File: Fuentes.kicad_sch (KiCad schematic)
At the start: 15 parts, among them J20 Conector 3V3, J21 Conector GND, J43 Conector GND, U1 LM2596S-ADJ, U2 LM1117-3.3

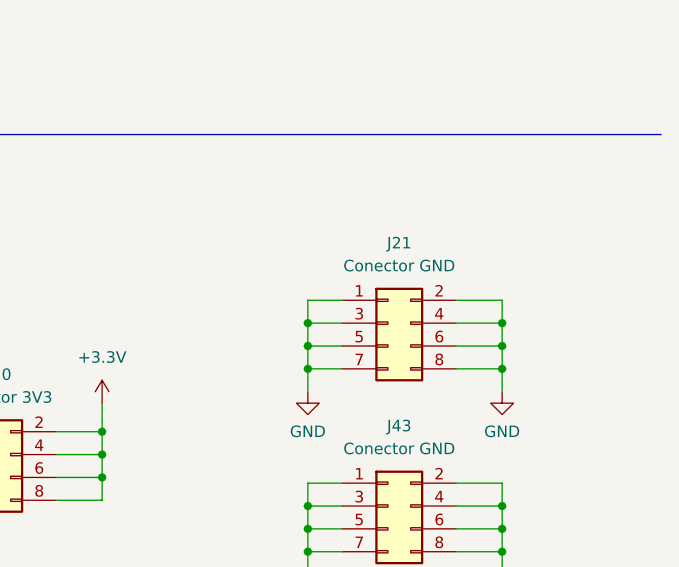
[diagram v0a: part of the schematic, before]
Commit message: Corrección de PCB.
Se agregaron algunos pin headers para conectar a GND algunos puntos. Se generaron los Gerber finales.
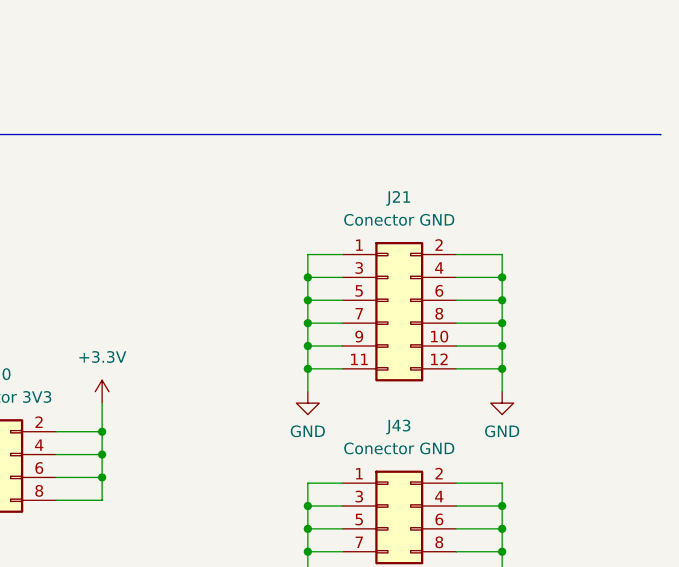
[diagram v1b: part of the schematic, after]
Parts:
- removed J21: Conector GND, Connector_PinHeader_2.54mm:PinHeader_2x04_P2.54mm_Vertical, symbol Connector_Generic:Conn_02x04_Odd_Even
- added J21: Conector GND, Connector_PinHeader_2.54mm:PinHeader_2x06_P2.54mm_Vertical, symbol Connector_Generic:Conn_02x06_Odd_Even
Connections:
- net GND: now also J21.1 (Pin_1), J21.10 (Pin_10), J21.11 (Pin_11), J21.12 (Pin_12), J21.2 (Pin_2), J21.3 (Pin_3), J21.4 (Pin_4), J21.5 (Pin_5), J21.6 (Pin_6), J21.7 (Pin_7), J21.8 (Pin_8), J21.9 (Pin_9)
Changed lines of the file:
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@@
   (junction (at 214.0204 67.31) (diameter 0) (color 0 0 0 0)
   )
+  (junction (at 245.745 109.855) (diameter 0) (color 0 0 0 0)
+  )
   (junction (at 245.745 132.715) (diameter 0) (color 0 0 0 0)
   )
@@
   (junction (at 129.54 67.31) (diameter 0) (color 0 0 0 0)
   )
+  (junction (at 267.335 107.315) (diameter 0) (color 0 0 0 0)
+  )
   (junction (at 267.335 114.935) (diameter 0) (color 0 0 0 0)
   )
@@
   (junction (at 168.91 67.31) (diameter 0) (color 0 0 0 0)
   )
+  (junction (at 267.335 109.855) (diameter 0) (color 0 0 0 0)
+  )
   (junction (at 222.885 129.54) (diameter 0) (color 0 0 0 0)
   )
+  (junction (at 245.745 107.315) (diameter 0) (color 0 0 0 0)
+  )
   (junction (at 267.335 112.395) (diameter 0) (color 0 0 0 0)
   )
+  (wire (pts (xy 249.555 104.775) (xy 245.745 104.775))
+    (stroke (width 0) (type default) (color 0 0 0 0))
+  )
   (wire (pts (xy 201.295 121.92) (xy 201.295 124.46))
     (stroke (width 0) (type default) (color 0 0 0 0))
@@
     (stroke (width 0) (type default) (color 0 0 0 0))
   )
+  (wire (pts (xy 267.335 104.775) (xy 267.335 107.315))
+    (stroke (width 0) (type default) (color 0 0 0 0))
+  )
   (wire (pts (xy 144.78 59.69) (xy 144.78 67.31))
     (stroke (width 0) (type default) (color 0 0 0 0))
   )
+  (wire (pts (xy 262.255 107.315) (xy 267.335 107.315))
+    (stroke (width 0) (type default) (color 0 0 0 0))
+  )
   (wire (pts (xy 262.255 137.795) (xy 267.335 137.795))
     (stroke (width 0) (type default) (color 0 0 0 0))
   )
+  (wire (pts (xy 249.555 107.315) (xy 245.745 107.315))
+    (stroke (width 0) (type default) (color 0 0 0 0))
+  )
   (wire (pts (xy 213.995 54.61) (xy 193.04 54.61))
     (stroke (width 0) (type default) (color 0 0 0 0))
@@
     (stroke (width 0) (type default) (color 0 0 0 0))
   )
+  (wire (pts (xy 245.745 104.775) (xy 245.745 107.315))
+    (stroke (width 0) (type default) (color 0 0 0 0))
+  )
   (wire (pts (xy 165.735 34.925) (xy 165.735 38.1))
     (stroke (width 0) (type default) (color 0 0 0 0))
@@
     (stroke (width 0) (type default) (color 0 0 0 0))
   )
+  (wire (pts (xy 245.745 107.315) (xy 245.745 109.855))
+    (stroke (width 0) (type default) (color 0 0 0 0))
+  )
   (wire (pts (xy 245.745 114.935) (xy 245.745 112.395))
     (stroke (width 0) (type default) (color 0 0 0 0))
@@
     (stroke (width 0) (type default) (color 0 0 0 0))
   )
+  (wire (pts (xy 267.335 107.315) (xy 267.335 109.855))
+    (stroke (width 0) (type default) (color 0 0 0 0))
+  )
   (wire (pts (xy 245.745 117.475) (xy 245.745 120.015))
     (stroke (width 0) (type default) (color 0 0 0 0))
@@
   )
   (wire (pts (xy 201.295 127) (xy 201.295 124.46))
+    (stroke (width 0) (type default) (color 0 0 0 0))
+  )
+  (wire (pts (xy 262.255 104.775) (xy 267.335 104.775))
     (stroke (width 0) (type default) (color 0 0 0 0))
   )
@@
     (pin "2")
   )
-  (symbol (lib_id "power:GND") (at 165.735 34.925 180) (unit 1)
-    (in_bom yes) (on_board yes) (fields_autoplaced)
-    (property "Reference" "#PWR012" (id 0) (at 165.735 28.575 0)
-      (effects (font (size 1.27 1.27)) hide)
-    )
-    (property "Value" "GND" (id 1) (at 167.64 33.6549 0)
-      (effects (font (size 1.27 1.27)) (justify right))
-    )
-    (property "Footprint" "" (id 2) (at 165.735 34.925 0)
-      (effects (font (size 1.27 1.27)) hide)
-    )
-    (property "Datasheet" "" (id 3) (at 165.735 34.925 0)
-      (effects (font (size 1.27 1.27)) hide)
-    )
-    (pin "1")
-  )
-  (symbol (lib_id "Regulator_Switching:LM2596S-ADJ") (at 144.78 52.07 0) (unit 1)
-    (in_bom yes) (on_board yes) (fields_autoplaced)
-    (property "Reference" "U1" (id 0) (at 144.78 41.91 0))
-    (property "Value" "LM2596S-ADJ" (id 1) (at 144.78 44.45 0))
-    (property "Footprint" "LM2596SX-ADJ_NOPB:LM2596SXADJNOPB" (id 2) (at 146.05 58.42 0)
-      (effects (font (size 1.27 1.27) italic) (justify left) hide)
-    )
-    (property "Datasheet" "http://www.ti.com/lit/ds/symlink/lm2596.pdf" (id 3) (at 144.78 52.07 0)
-      (effects (font (size 1.27 1.27)) hide)
-    )
-    (pin "1")
-    (pin "2")
-    (pin "3")
-    (pin "4")
-    (pin "5")
-  )
-  (symbol (lib_id "power:PWR_FLAG") (at 90.805 67.31 180) (unit 1)
-    (in_bom yes) (on_board yes) (fields_autoplaced)
-    (property "Reference" "#FLG02" (id 0) (at 90.805 69.215 0)
-      (effects (font (size 1.27 1.27)) hide)
-    )
-    (property "Value" "PWR_FLAG" (id 1) (at 92.71 68.5799 0)
-      (effects (font (size 1.27 1.27)) (justify right))
-    )
-    (property "Footprint" "" (id 2) (at 90.805 67.31 0)
-      (effects (font (size 1.27 1.27)) hide)
-    )
-    (property "Datasheet" "~" (id 3) (at 90.805 67.31 0)
-      (effects (font (size 1.27 1.27)) hide)
-    )
-    (pin "1")
-  )
-  (symbol (lib_id "Connector_Generic:Conn_02x04_Odd_Even") (at 254.635 112.395 0) (unit 1)
-    (in_bom yes) (on_board yes) (fields_autoplaced)
-    (property "Reference" "J21" (id 0) (at 255.905 103.505 0))
-    (property "Value" "Conector GND" (id 1) (at 255.905 106.045 0))
-    (property "Footprint" "Connector_PinHeader_2.54mm:PinHeader_2x04_P2.54mm_Vertical" (id 2) (at 254.635 112.395 0)
-      (effects (font (size 1.27 1.27)) hide)
-    )
-    (property "Datasheet" "~" (id 3) (at 254.635 112.395 0)
-      (effects (font (size 1.27 1.27)) hide)
-    )
-    (pin "1")
+  (symbol (lib_id "Connector_Generic:Conn_02x06_Odd_Even") (at 254.635 109.855 0) (unit 1)
+    (in_bom yes) (on_board yes) (fields_autoplaced)
+    (property "Reference" "J21" (id 0) (at 255.905 98.425 0))
+    (property "Value" "Conector GND" (id 1) (at 255.905 100.965 0))
+    (property "Footprint" "Connector_PinHeader_2.54mm:PinHeader_2x06_P2.54mm_Vertical" (id 2) (at 254.635 109.855 0)
+      (effects (font (size 1.27 1.27)) hide)
+    )
+    (property "Datasheet" "~" (id 3) (at 254.635 109.855 0)
+      (effects (font (size 1.27 1.27)) hide)
+    )
+    (pin "1")
+    (pin "10")
+    (pin "11")
+    (pin "12")
     (pin "2")
     (pin "3")
@@
     (pin "7")
     (pin "8")
+    (pin "9")
+  )
+  (symbol (lib_id "power:GND") (at 165.735 34.925 180) (unit 1)
+    (in_bom yes) (on_board yes) (fields_autoplaced)
+    (property "Reference" "#PWR012" (id 0) (at 165.735 28.575 0)
+      (effects (font (size 1.27 1.27)) hide)
+    )
+    (property "Value" "GND" (id 1) (at 167.64 33.6549 0)
+      (effects (font (size 1.27 1.27)) (justify right))
+    )
+    (property "Footprint" "" (id 2) (at 165.735 34.925 0)
+      (effects (font (size 1.27 1.27)) hide)
+    )
+    (property "Datasheet" "" (id 3) (at 165.735 34.925 0)
+      (effects (font (size 1.27 1.27)) hide)
+    )
+    (pin "1")
+  )
+  (symbol (lib_id "Regulator_Switching:LM2596S-ADJ") (at 144.78 52.07 0) (unit 1)
+    (in_bom yes) (on_board yes) (fields_autoplaced)
+    (property "Reference" "U1" (id 0) (at 144.78 41.91 0))
+    (property "Value" "LM2596S-ADJ" (id 1) (at 144.78 44.45 0))
+    (property "Footprint" "LM2596SX-ADJ_NOPB:LM2596SXADJNOPB" (id 2) (at 146.05 58.42 0)
+      (effects (font (size 1.27 1.27) italic) (justify left) hide)
+    )
+    (property "Datasheet" "http://www.ti.com/lit/ds/symlink/lm2596.pdf" (id 3) (at 144.78 52.07 0)
+      (effects (font (size 1.27 1.27)) hide)
+    )
+    (pin "1")
+    (pin "2")
+    (pin "3")
+    (pin "4")
+    (pin "5")
+  )
+  (symbol (lib_id "power:PWR_FLAG") (at 90.805 67.31 180) (unit 1)
+    (in_bom yes) (on_board yes) (fields_autoplaced)
+    (property "Reference" "#FLG02" (id 0) (at 90.805 69.215 0)
+      (effects (font (size 1.27 1.27)) hide)
+    )
+    (property "Value" "PWR_FLAG" (id 1) (at 92.71 68.5799 0)
+      (effects (font (size 1.27 1.27)) (justify right))
+    )
+    (property "Footprint" "" (id 2) (at 90.805 67.31 0)
+      (effects (font (size 1.27 1.27)) hide)
+    )
+    (property "Datasheet" "~" (id 3) (at 90.805 67.31 0)
+      (effects (font (size 1.27 1.27)) hide)
+    )
+    (pin "1")
   )
   (symbol (lib_id "power:+3.3V") (at 201.295 121.92 0) (unit 1)
